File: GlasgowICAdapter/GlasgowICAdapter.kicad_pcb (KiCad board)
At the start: 2 copper layers, 80 x 49 mm, 19 parts, among them J1 PORT A, J10 PORT A IO, J11 PORT B IO, J2 PORT B, J3 ZIF_SOCKET, J4 EN_U1, J5 EN_U2, J6 ZIF_IO_LEFT, J7 EN_U3, J8 EN_U4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

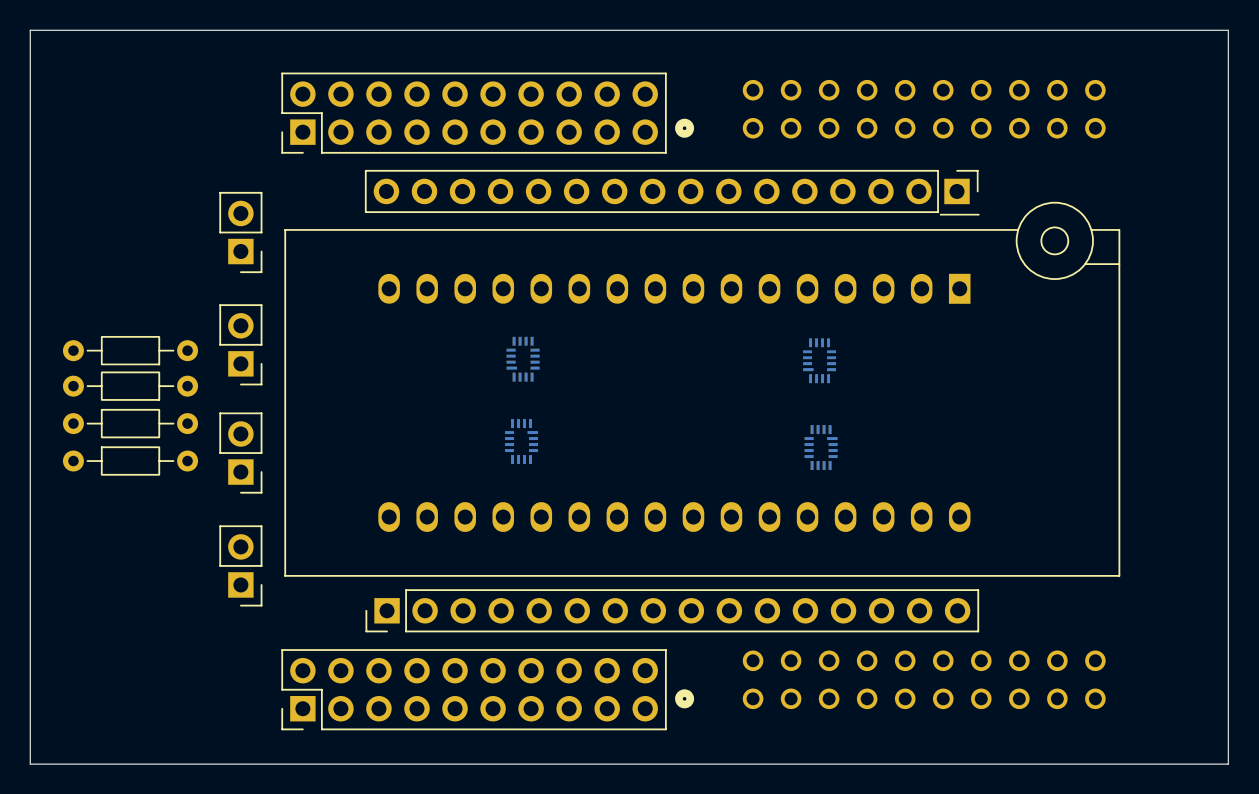
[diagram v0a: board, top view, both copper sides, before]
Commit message: Added PCB holes
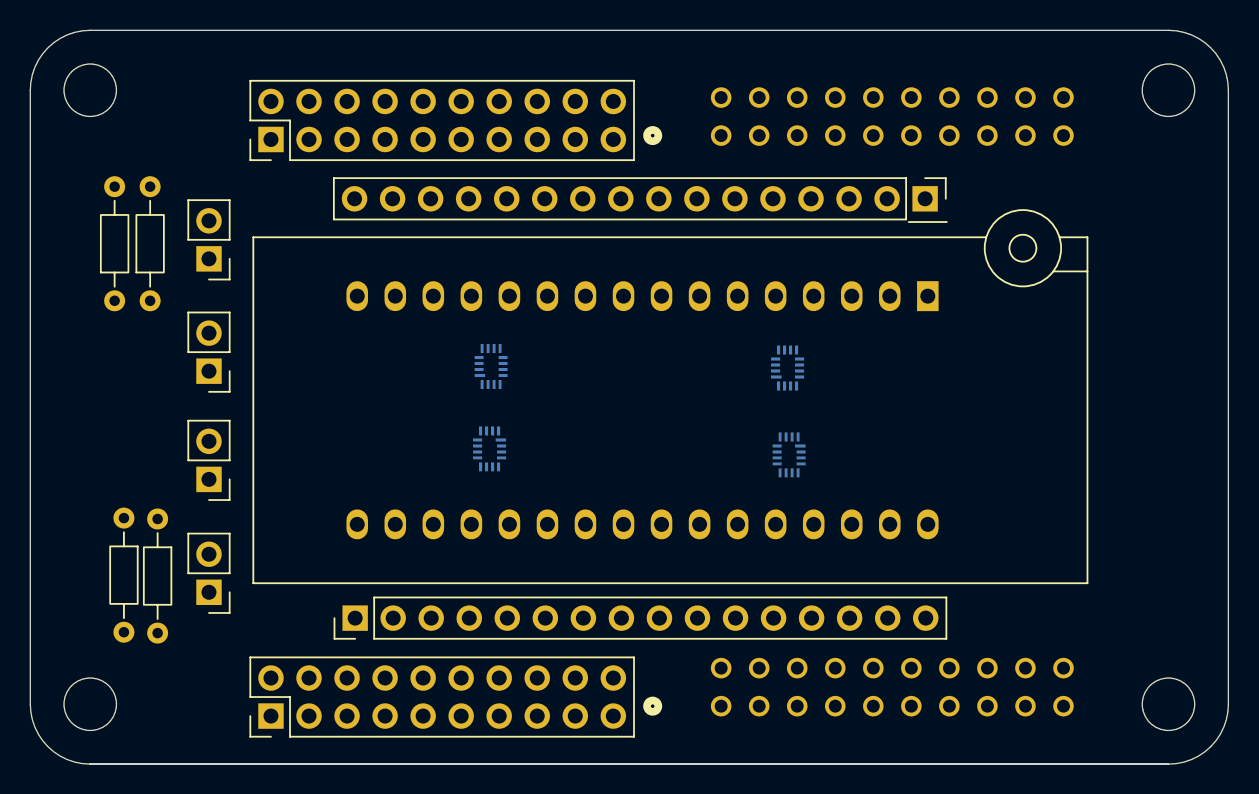
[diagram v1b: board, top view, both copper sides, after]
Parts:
- moved R2 7.50 mm to (93.6, 94.1), turned to 90 degrees
- moved R3 7.15 mm to (94.2, 108.6), turned to -90 degrees
- moved R4 6.82 mm to (96.5, 108.6), turned to -90 degrees
- moved R1 4.16 mm to (96.0, 94.1), turned to 90 degrees
- moved J10 2.19 mm to (104.1, 83.3)
- moved J11 2.19 mm to (104.1, 121.8)
- moved J4 2.19 mm to (99.9, 91.3)
- moved J5 2.19 mm to (99.9, 98.8)
- moved J8 2.19 mm to (99.9, 113.5)
- moved U1 2.19 mm to (138.6, 98.5)
- moved U2 2.19 mm to (118.8, 98.5)
- moved U5 2.19 mm to (138.7, 104.4)
- moved J1 2.19 mm to (134.1, 83.0)
- moved J2 2.19 mm to (134.1, 121.1)
- moved J3 2.19 mm to (147.9, 93.8)
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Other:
- outline, holes or cut-outs redrawn

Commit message: Finished PCB routing, finally :D
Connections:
- U1 pad 1: GND -> unconnected-(U1-NC-Pad1)
- U2 pad 1: GND -> unconnected-(U2-NC-Pad1)
- U4 pad 1: GND -> unconnected-(U4-NC-Pad1)
- U5 pad 1: GND -> unconnected-(U5-NC-Pad1)
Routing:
- net GND: track 0.00 -> 210.0 mm
- net VIOB: track 0.00 -> 116.8 mm, vias 0 -> 4
- net VIOA: track 0.00 -> 97.0 mm, vias 0 -> 3
- net PA0: track 0.00 -> 82.6 mm, vias 0 -> 2
- net PB0: track 0.00 -> 79.6 mm, vias 0 -> 2
- net PB1: track 0.00 -> 77.1 mm, vias 0 -> 5
- net PA1: track 0.00 -> 67.6 mm, vias 0 -> 2
- net PA2: track 0.00 -> 60.9 mm, vias 0 -> 1
- net Net-(J8-Pin_1): track 0.00 -> 55.8 mm, vias 0 -> 1
- net PA3: track 0.00 -> 55.7 mm, vias 0 -> 3
- net PB3: track 0.00 -> 55.4 mm, vias 0 -> 3
- net PB2: track 0.00 -> 50.7 mm, vias 0 -> 1
- net PB5: track 0.00 -> 49.7 mm, vias 0 -> 3
- net PB4: track 0.00 -> 49.4 mm, vias 0 -> 1
- net Net-(J4-Pin_1): track 0.00 -> 47.0 mm, vias 0 -> 2
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
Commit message: Fixed PCB a little bit
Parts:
- moved U5 1.36 mm to (137.5, 103.6)
- moved J4 1.36 mm to (98.8, 90.5)
- moved J5 1.36 mm to (98.8, 98.0)
- moved J7 1.36 mm to (98.8, 105.2)
- moved J8 1.36 mm to (98.8, 112.8)
- moved J1 1.36 mm to (133.0, 82.3)
- moved J10 1.36 mm to (102.9, 82.5)
- moved J11 1.36 mm to (102.9, 121.0)
- moved J2 1.36 mm to (133.0, 120.4)
- moved J3 1.36 mm to (146.8, 93.0)
- moved J6 1.36 mm to (146.6, 86.5)
- moved J9 1.36 mm to (108.6, 114.5)
- moved R1 1.36 mm to (94.9, 93.3)
- moved R2 1.36 mm to (92.5, 93.3)
- moved R3 1.36 mm to (93.1, 107.8)
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
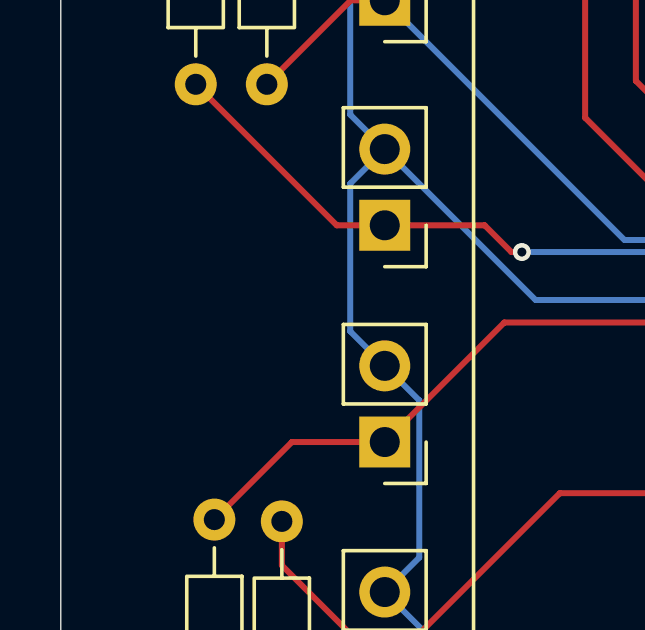
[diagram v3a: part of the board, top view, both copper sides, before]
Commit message: Added silkscreens
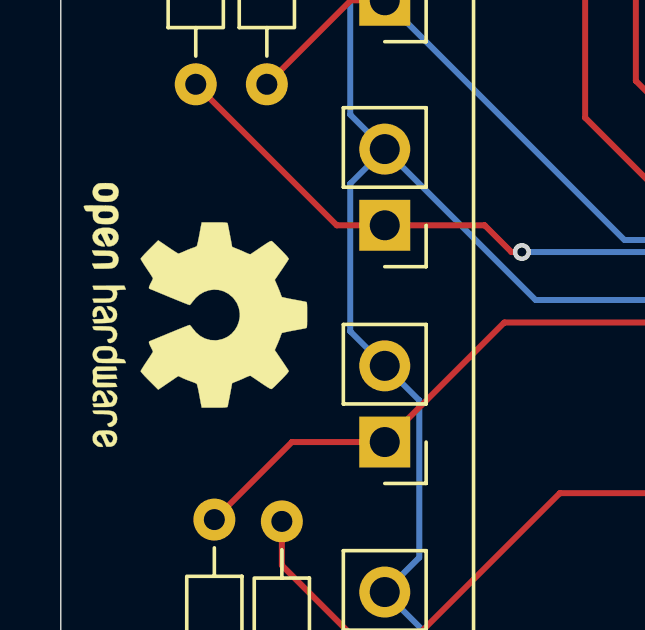
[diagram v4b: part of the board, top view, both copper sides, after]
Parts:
- added G***: LOGO, SFH11_PBPC_D10_ST_BK:GoblinCatLogo, B.Cu at (153.5, 100.5)
- added REF**: OSHW-Logo2_9.8x8mm_SilkScreen, Symbol:OSHW-Logo2_9.8x8mm_SilkScreen, F.Cu at (92.5, 101.0)
